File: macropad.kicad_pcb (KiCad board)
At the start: 2 copper layers, 66 x 45.7 mm, 14 parts, among them J1 Conn_01x03_Pin, J2 Conn_01x02_Pin, SW1 SW_Push, SW2 SW_Push, SW3 SW_Push, U1 XIAO-RP2040-DIP

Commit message: Add brightness adjust and edit firmware
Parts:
- added RV1: R_Potentiometer, Potentiometer_THT:Potentiometer_Vishay_T73YP_Vertical, F.Cu at (167.4, 73.2)
- moved J1 1.52 mm to (136.9, 84.8)
- moved J2 1.52 mm to (147.6, 84.8)
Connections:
- D1 pad C: GND -> Adjusted GND
- D2 pad C: GND -> Adjusted GND
- D3 pad C: GND -> Adjusted GND
- D4 pad C: GND -> Adjusted GND
- J2 pad 2: Power -> +5V
- U1 pad 14: unconnected-(U1-VBUS-Pad14)_1 -> +5V
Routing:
- net +5V: track 0.00 -> 52.4 mm
- net Adjusted GND: track 0.00 -> 42.5 mm
- net Power: track 45.3 -> 34.7 mm
- net GND: track 140.8 -> 130.7 mm, vias 0 -> 1
- net IO2: track 14.9 -> 13.3 mm
- net IO4: track 23.3 -> 21.8 mm
- net IO3: track 23.0 -> 21.5 mm
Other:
- board text added: "Brightness Adjust"
- board text added: "Indicators"
- board text added: "Press & hold any key until LEDs light up to enable GPIO control."

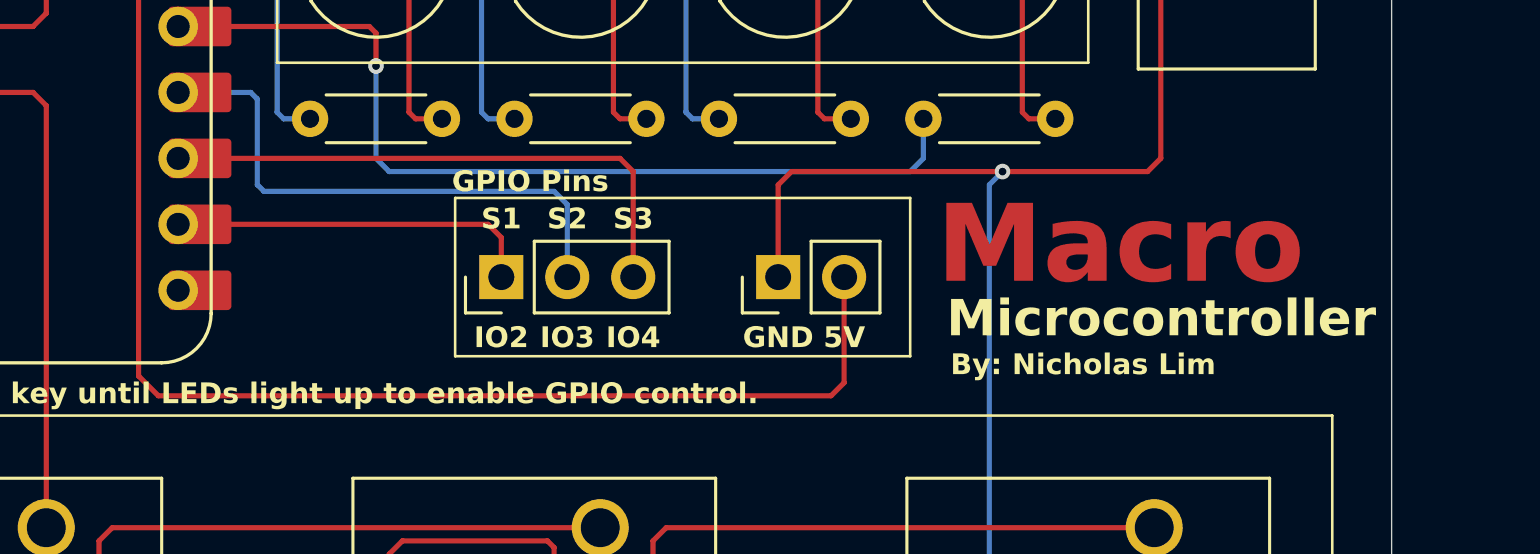
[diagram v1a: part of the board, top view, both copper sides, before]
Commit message: Edit placement of pins
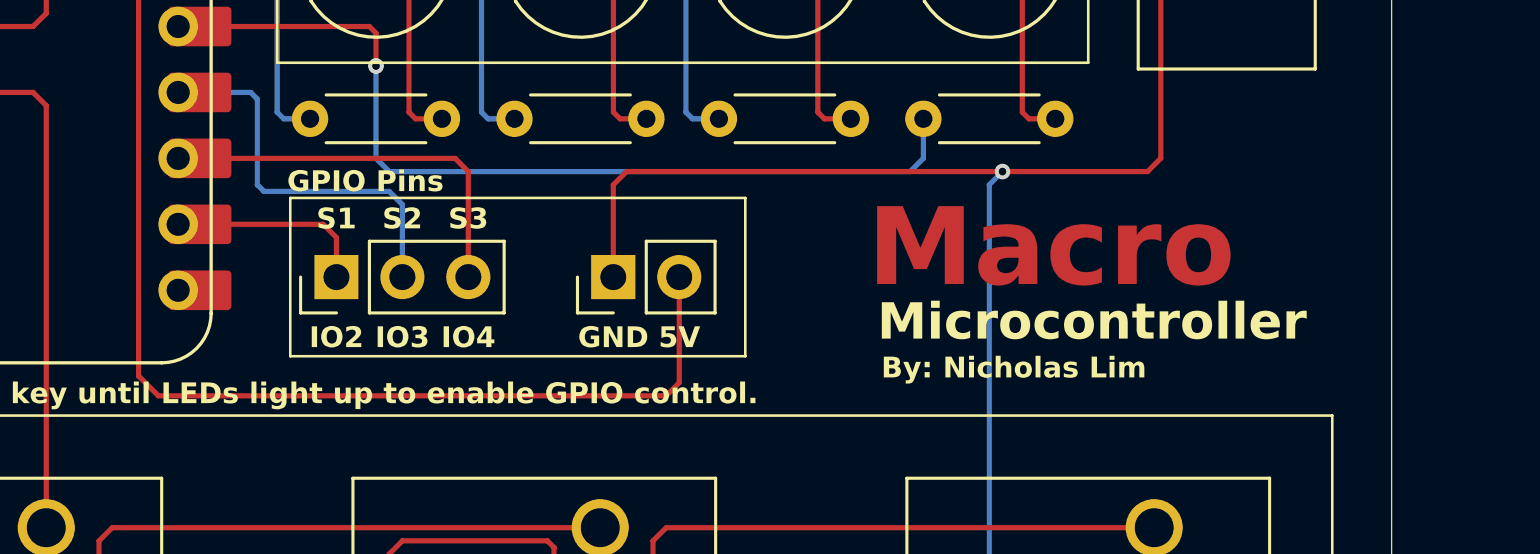
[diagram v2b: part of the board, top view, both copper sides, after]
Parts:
- moved J1 6.35 mm to (130.6, 84.8)
- moved J2 6.35 mm to (141.2, 84.8)
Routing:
- net +5V: track 52.4 -> 46.0 mm
- net IO4: track 21.8 -> 15.5 mm
- net IO3: track 21.5 -> 15.2 mm
- net GND: track 130.7 -> 137.0 mm
- net IO2: track 13.3 -> 7.00 mm
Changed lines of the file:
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@@
 	(footprint "Connector_PinHeader_2.54mm:PinHeader_1x02_P2.54mm_Vertical"
 		(layer "F.Cu")
-		(at 147.569 84.836 90)
+		(at 141.219 84.836 90)
 		(descr "Through hole straight pin header, 1x02, 2.54mm pitch, single row")
 		(tags "Through hole pin header THT 1x02 2.54mm single row")
@@
 	(footprint "Connector_PinHeader_2.54mm:PinHeader_1x03_P2.54mm_Vertical"
 		(layer "F.Cu")
-		(at 136.906 84.836 90)
+		(at 130.556 84.836 90)
 		(descr "Through hole straight pin header, 1x03, 2.54mm pitch, single row")
 		(tags "Through hole pin header THT 1x03 2.54mm single row")
@@
 	)
 	(gr_rect
-		(start 135.128 81.788)
-		(end 152.654 87.884)
+		(start 128.778 81.788)
+		(end 146.304 87.884)
 		(stroke
 			(width 0.1)
@@
 	)
 	(gr_text "Macro"
-		(at 153.67 85.344 0)
+		(at 151.003 85.471 0)
 		(layer "F.Cu")
 		(effects
@@
 	)
 	(gr_text "Macro"
-		(at 153.67 85.344 0)
+		(at 151.003 85.471 0)
 		(layer "F.Mask")
 		(effects
@@
 	)
 	(gr_text "5V"
-		(at 150.114 87.63 0)
+		(at 143.764 87.63 0)
 		(layer "F.SilkS")
 		(effects
@@
 	)
 	(gr_text "S2"
-		(at 139.446 83.058 0)
+		(at 133.096 83.058 0)
 		(layer "F.SilkS")
 		(effects
@@
 	)
 	(gr_text "S1"
-		(at 136.906 83.058 0)
+		(at 130.556 83.058 0)
 		(layer "F.SilkS")
 		(effects
@@
 	)
 	(gr_text "IO4"
-		(at 141.986 87.63 0)
+		(at 135.636 87.63 0)
 		(layer "F.SilkS")
 		(effects
@@
 	)
 	(gr_text "GPIO Pins"
-		(at 135.001 81.153 0)
+		(at 128.651 81.153 0)
 		(layer "F.SilkS")
 		(effects
@@
 	)
 	(gr_text "By: Nicholas Lim"
-		(at 154.2034 88.6714 0)
+		(at 151.5364 88.7984 0)
 		(layer "F.SilkS")
 		(effects
@@
 	)
 	(gr_text "IO2\n"
-		(at 136.906 87.63 0)
+		(at 130.556 87.63 0)
 		(layer "F.SilkS")
 		(effects
@@
 	)
 	(gr_text "Microcontroller"
-		(at 154.051 87.249 0)
+		(at 151.384 87.376 0)
 		(layer "F.SilkS")
 		(effects
@@
 	)
 	(gr_text "GND"
-		(at 147.569 87.63 0)
+		(at 141.219 87.63 0)
 		(layer "F.SilkS")
 		(effects
@@
 	)
 	(gr_text "IO3"
-		(at 139.446 87.63 0)
+		(at 133.096 87.63 0)
 		(layer "F.SilkS")
 		(effects
@@
 	)
 	(gr_text "S3\n"
-		(at 141.986 83.058 0)
+		(at 135.636 83.058 0)
 		(layer "F.SilkS")
 		(effects
@@
 	(segment
 		(start 156.21 80.772)
-		(end 148.082 80.772)
+		(end 141.732 80.772)
 		(width 0.2)
 		(layer "F.Cu")
@@
 	)
 	(segment
-		(start 162.306 73.152)
-		(end 162.306 80.264)
+		(start 141.219 81.285)
+		(end 141.732 80.772)
 		(width 0.2)
 		(layer "F.Cu")
@@
 	)
 	(segment
-		(start 147.569 84.836)
-		(end 147.569 81.285)
+		(start 162.306 73.152)
+		(end 162.306 80.264)
 		(width 0.2)
 		(layer "F.Cu")
@@
 	)
 	(segment
-		(start 148.082 80.772)
-		(end 147.569 81.285)
+		(start 141.219 84.836)
+		(end 141.219 81.285)
 		(width 0.2)
 		(layer "F.Cu")
@@
 	)
 	(segment
-		(start 123.444 70.104)
-		(end 125.295 70.104)
+		(start 143.759 88.905)
+		(end 143.256 89.408)
 		(width 0.2)
 		(layer "F.Cu")
@@
 	)
 	(segment
-		(start 122.936 88.646)
-		(end 122.936 70.612)
+		(start 143.759 84.836)
+		(end 143.759 88.905)
 		(width 0.2)
 		(layer "F.Cu")
@@
 	)
 	(segment
-		(start 150.109 84.836)
-		(end 150.109 88.905)
+		(start 123.444 70.104)
+		(end 125.295 70.104)
 		(width 0.2)
 		(layer "F.Cu")
@@
 	)
 	(segment
-		(start 123.698 89.408)
-		(end 122.936 88.646)
+		(start 122.936 88.646)
+		(end 122.936 70.612)
 		(width 0.2)
 		(layer "F.Cu")
@@
 	)
 	(segment
-		(start 150.109 88.905)
-		(end 149.606 89.408)
+		(start 123.698 89.408)
+		(end 122.936 88.646)
 		(width 0.2)
 		(layer "F.Cu")
@@
 	)
 	(segment
-		(start 149.606 89.408)
+		(start 143.256 89.408)
 		(end 123.698 89.408)
 		(width 0.2)
@@
 	)
 	(segment
-		(start 138.938 81.534)
-		(end 139.446 82.042)
-		(width 0.2)
-		(layer "B.Cu")
-		(net 15)
-	)
-	(segment
-		(start 139.446 82.042)
-		(end 139.446 84.836)
+		(start 133.096 82.042)
+		(end 132.588 81.534)
 		(width 0.2)
 		(layer "B.Cu")
@@
 	)
 	(segment
-		(start 127.762 81.534)
-		(end 138.938 81.534)
+		(start 127.508 77.978)
+		(end 127.508 81.28)
 		(width 0.2)
 		(layer "B.Cu")
@@
 	)
 	(segment
-		(start 127.508 77.978)
-		(end 127.508 81.28)
+		(start 133.096 84.836)
+		(end 133.096 82.042)
 		(width 0.2)
 		(layer "B.Cu")
@@
 	)
 	(segment
-		(start 141.986 80.772)
-		(end 141.986 84.836)
+		(start 127.762 81.534)
+		(end 132.588 81.534)
+		(width 0.2)
+		(layer "B.Cu")
+		(net 15)
+	)
+	(segment
+		(start 135.636 84.836)
+		(end 135.636 80.772)
 		(width 0.2)
 		(layer "F.Cu")
@@
 	)
 	(segment
-		(start 141.478 80.264)
-		(end 141.986 80.772)
+		(start 124.46 80.264)
+		(end 135.128 80.264)
 		(width 0.2)
 		(layer "F.Cu")
@@
 	)
 	(segment
-		(start 124.46 80.264)
-		(end 141.478 80.264)
+		(start 135.636 80.772)
+		(end 135.128 80.264)
 		(width 0.2)
 		(layer "F.Cu")
@@
 	)
 	(segment
-		(start 136.906 83.312)
-		(end 136.398 82.804)
+		(start 130.556 83.312)
+		(end 130.048 82.804)
 		(width 0.2)
 		(layer "F.Cu")
@@
 	)
 	(segment
-		(start 136.906 84.836)
-		(end 136.906 83.312)
+		(start 130.048 82.804)
+		(end 125.295 82.804)
 		(width 0.2)
 		(layer "F.Cu")
@@
 	)
 	(segment
-		(start 136.398 82.804)
-		(end 125.295 82.804)
+		(start 130.556 84.836)
+		(end 130.556 83.312)
 		(width 0.2)
 		(layer "F.Cu")
